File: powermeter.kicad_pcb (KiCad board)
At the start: 2 copper layers, 17.8 x 21.1 mm, 21 parts, among them J1 Conn_01x04, J2 Conn_01x07, J3 Conn_01x07, Q1 S8550, U1 XIAO BLE, U2 HX711, U3 MPU-6050

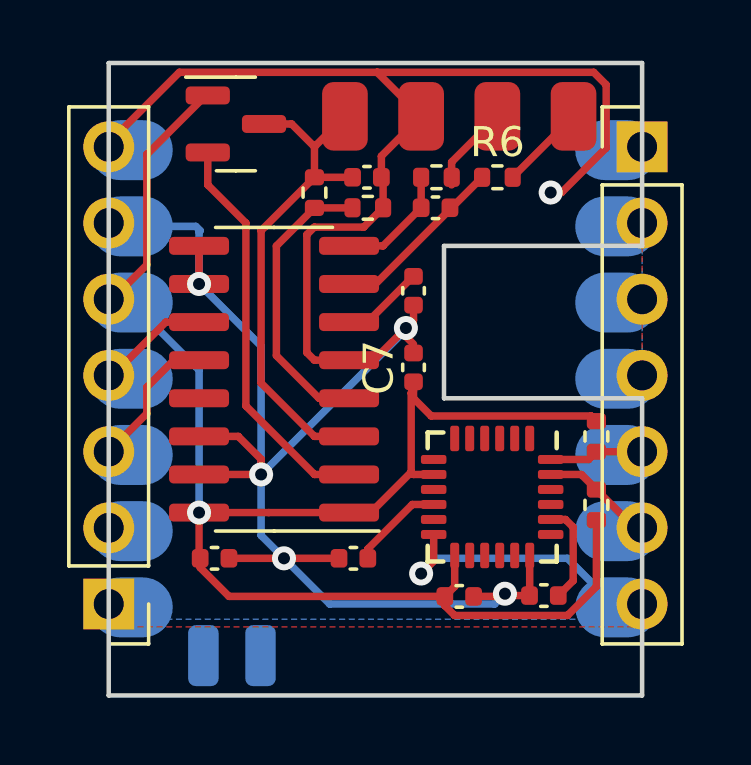
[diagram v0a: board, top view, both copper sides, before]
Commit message: Fix 5v-GND short. Minor tweaks on layout
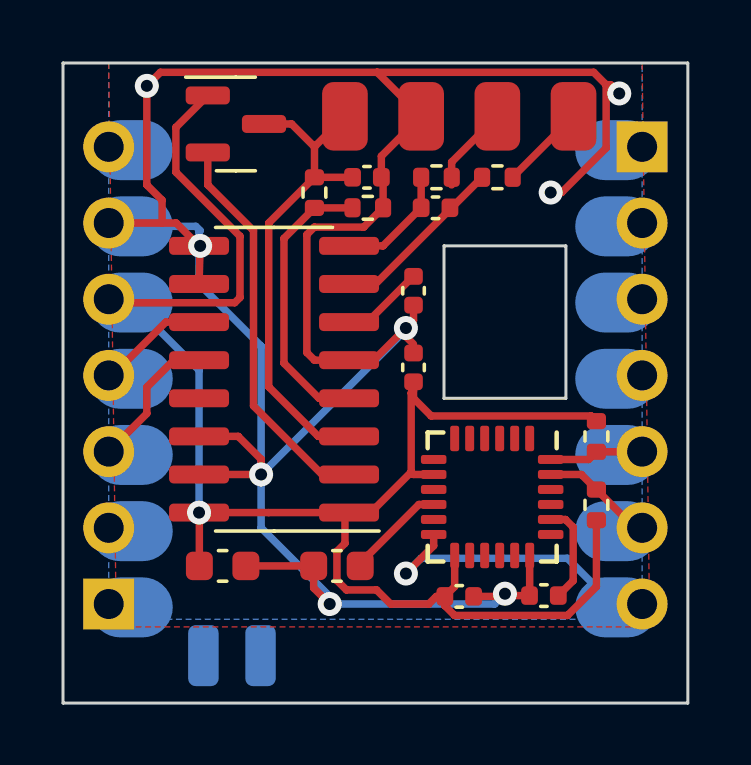
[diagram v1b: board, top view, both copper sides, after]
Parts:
- C3, C6: footprint Capacitor_SMD:C_0402_1005Metric -> Capacitor_SMD:C_0603_1608Metric
- moved C6 0.60 mm to (59.4, 57.7)
- moved C3 0.37 mm to (55.6, 57.7)
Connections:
- J3 pad 7: GND -> /5V
- U1 pad 14: GND -> /5V
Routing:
- net GND: track 83.2 -> 89.8 mm, vias 6 -> 8
- net +3.3V: track 53.9 -> 56.3 mm
- net /MPU_INT: track 8.87 -> 9.59 mm
- net Net-(J1-Pin_1): track 17.3 -> 16.7 mm
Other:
- board size 17.8 x 21.1 mm -> 20.8 x 21.3 mm
- rule pad_to_mask_clearance: 0 -> 0.038

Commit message: Fix AD0 MPU6050 to GND
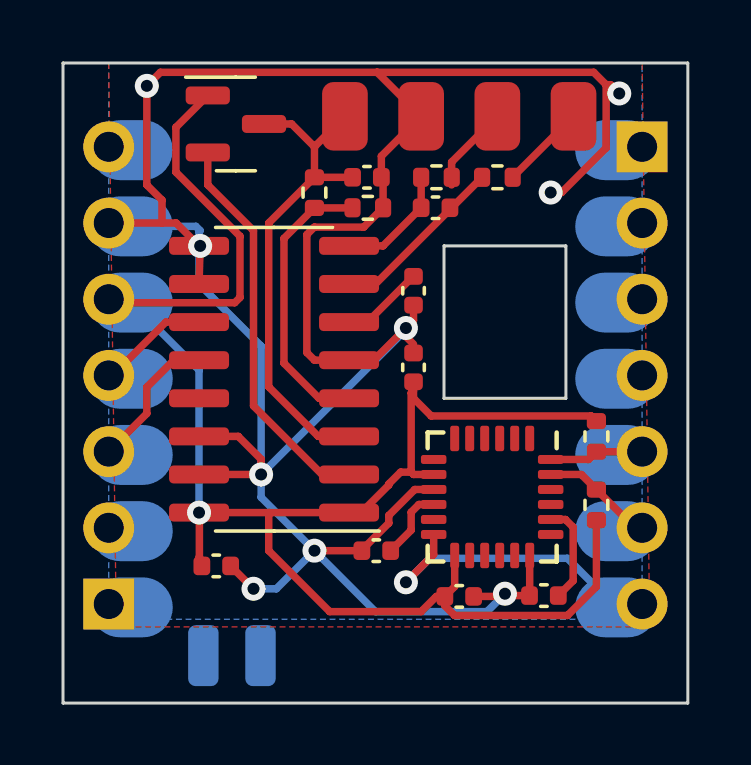
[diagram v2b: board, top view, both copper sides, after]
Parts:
- C3, C6: footprint Capacitor_SMD:C_0603_1608Metric -> Capacitor_SMD:C_0402_1005Metric
- moved C6 1.41 mm to (60.7, 57.1)
- moved C3 0.21 mm to (55.4, 57.7)
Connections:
- U3 pad 9: unconnected-(U3-AD0-Pad9) -> GND
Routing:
- net GND: track 89.8 -> 94.2 mm, vias 8 -> 9
- net +3.3V: track 56.3 -> 58.1 mm
- net Net-(U3-REGOUT): track 3.24 -> 2.42 mm

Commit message: Change MPU6050 to LIS6DS3TRC
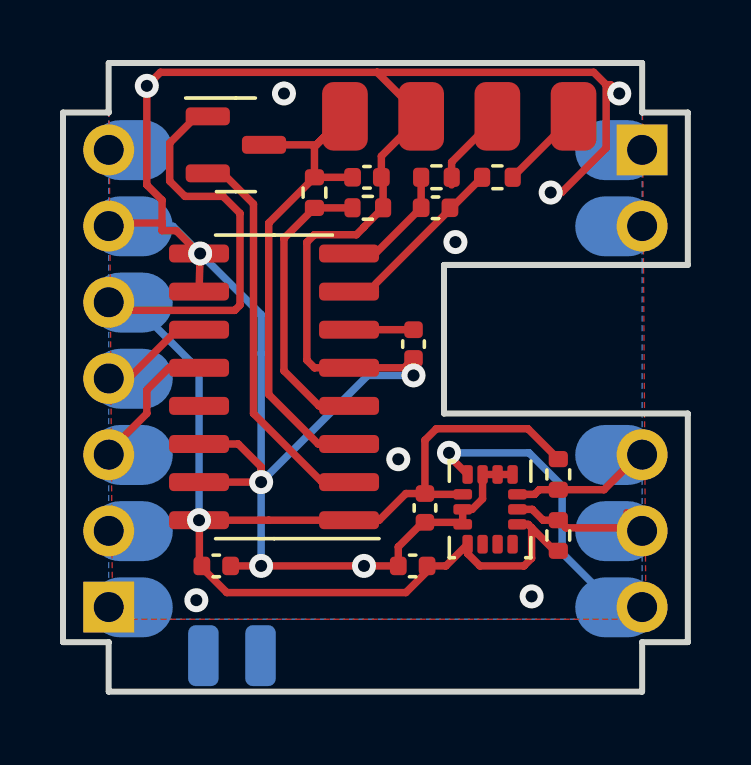
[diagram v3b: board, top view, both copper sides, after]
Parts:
- removed C7: 0.1uF, Capacitor_SMD:C_0402_1005Metric
- removed C8: 10nF, Capacitor_SMD:C_0402_1005Metric
- C5: value 2.2nF -> 0.1uF
- U3: value MPU-6050 -> LSM6DS3; footprint Sensor_Motion:InvenSense_QFN-24_4x4mm_P0.5mm -> Package_LGA:LGA-14_3x2.5mm_P0.5mm_LayoutBorder3x4y
- moved C5 4.48 mm to (61.9, 57.7), turned to 0 degrees
- moved C6 2.16 mm to (62.4, 55.7), turned to -90 degrees
- moved R4 1.79 mm to (66.8, 54.6)
- moved C2 1.78 mm to (62.0, 50.3)
- moved R5 1.63 mm to (66.8, 56.6)
- moved Q1 0.70 mm to (56.1, 43.6)
- moved U3 0.42 mm to (64.5, 55.8)
- moved U2 0.25 mm to (57.3, 51.7)
- moved J3 0.10 mm to (51.8, 59.0)
- moved J2 0.10 mm to (69.6, 43.8)
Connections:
- C5 pad 1: Net-(U3-CPOUT) -> GND
- C5 pad 2: GND -> +3.3V
- C6 pad 1: Net-(U3-REGOUT) -> +3.3V
- U3 pad 1: unconnected-(U3-CLKIN-Pad1) -> GND
- U3 pad 10: Net-(U3-REGOUT) -> unconnected-(U3-NC-Pad10)
- U3 pad 12: /MPU_INT -> +3.3V
- U3 pad 13: +3.3V -> /SCL
- U3 pad 14: unconnected-(U3-NC-Pad14) -> /SDA
- U3 pad 2: unconnected-(U3-NC-Pad2) -> GND
- U3 pad 3: unconnected-(U3-NC-Pad3) -> GND
- U3 pad 4: unconnected-(U3-NC-Pad4) -> /MPU_INT
- U3 pad 5: unconnected-(U3-NC-Pad5) -> +3.3V
- U3 pad 6: unconnected-(U3-AUX_DA-Pad6) -> GND
- U3 pad 7: unconnected-(U3-AUX_CL-Pad7) -> GND
- U3 pad 9: GND -> unconnected-(U3-INT2-Pad9)
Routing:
- net GND: track 94.2 -> 85.3 mm, vias 9 -> 13
- net +3.3V: track 58.1 -> 54.7 mm
- net Net-(U3-CPOUT): track 3.34 -> 0.00 mm
- net Net-(U3-REGOUT): track 2.42 -> 0.00 mm
- net /SDA: track 2.82 -> 4.75 mm
- net /SCL: track 3.53 -> 5.15 mm
- net Net-(J1-Pin_1): track 16.7 -> 18.0 mm
- net Net-(U2-VBG): track 2.78 -> 2.15 mm
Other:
- board size 20.8 x 21.3 mm -> 20.8 x 21 mm
